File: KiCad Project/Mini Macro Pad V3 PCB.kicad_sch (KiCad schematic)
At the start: 98 parts, among them J1 USB_C_Receptacle_USB2.0_14P, SW1 SW_Push bootsel, SW10 SW_Push, SW11 SW_Push, SW12 SW_Push, SW13 SW_Push, SW14 SW_Push, SW15 SW_Push, SW16 SW_Push, SW17 SW_Push, SW18 SW_Push, SW19 SW_Push, SW2 SW_Push, SW20 SW_Push, SW21 SW_Push, SW22 RotaryEncoder_Switch_MP, SW23 RotaryEncoder_Switch_MP, SW3 SW_Push, SW4 SW_Push, SW5 SW_Push, SW6 SW_Push, SW7 SW_Push, SW8 SW_Push, SW9 SW_Push, U1 RP2040, U2 NCP1117-3.3_SOT223, U3 W25Q128JVS, Y1 ABM8-272-T3

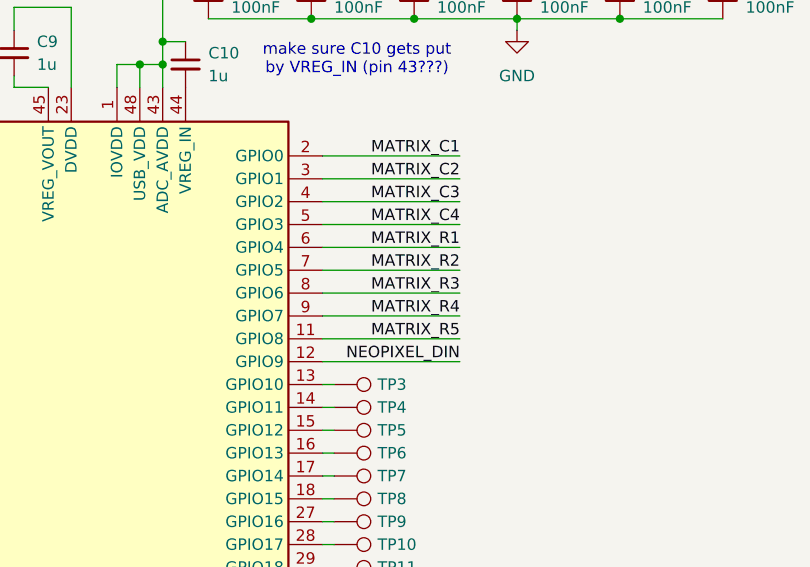
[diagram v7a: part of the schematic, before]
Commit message: changed some GPIO connections & did more trace routing
Reversed the order that C1 to C5 connect in
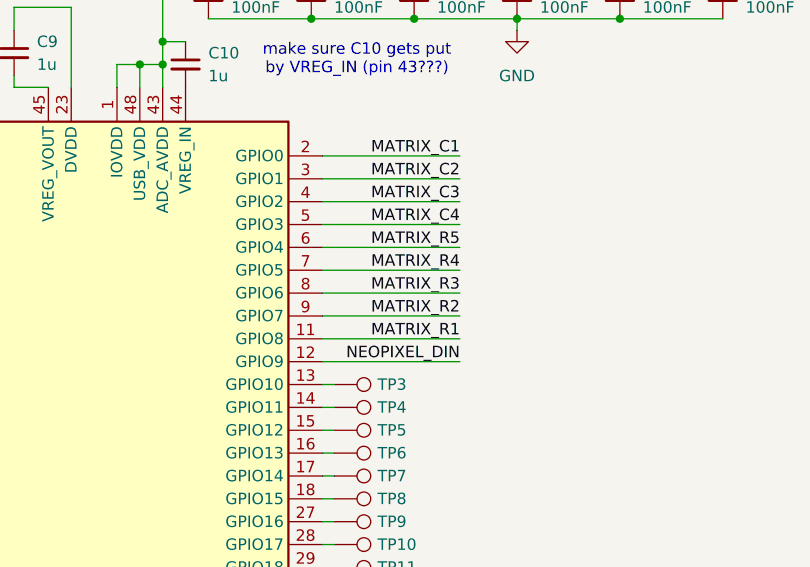
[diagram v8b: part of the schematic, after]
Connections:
- net MATRIX_R1: now also U1.11 (GPIO8); no longer U1.6 (GPIO4)
- net MATRIX_R2: now also U1.9 (GPIO7); no longer U1.7 (GPIO5)
- net MATRIX_R4: now also U1.7 (GPIO5); no longer U1.9 (GPIO7)
- net MATRIX_R5: now also U1.6 (GPIO4); no longer U1.11 (GPIO8)
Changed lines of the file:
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@@
+		)
+	)
+	(label "MATRIX_R2"
+		(at 246.38 88.9 180)
+		(effects
+			(font
+				(size 1.27 1.27)
+			)
+			(justify right bottom)
 		)
 	)
@@
 		)
 	)
-	(label "MATRIX_R4"
-		(at 246.38 88.9 180)
+	(label "MATRIX_R3"
+		(at 246.38 86.36 180)
 		(effects
 			(font
@@
 		)
 	)
-	(label "MATRIX_R5"
-		(at 246.38 91.44 180)
-		(effects
-			(font
-				(size 1.27 1.27)
-			)
-			(justify right bottom)
-		)
-	)
 	(label "MATRIX_C1"
 		(at 96.52 140.97 270)
@@
 		)
 	)
+	(label "MATRIX_R4"
+		(at 246.38 83.82 180)
+		(effects
+			(font
+				(size 1.27 1.27)
+			)
+			(justify right bottom)
+		)
+	)
 	(label "USB_D-"
 		(at 54.61 167.64 180)
@@
 	)
 	(label "MATRIX_R1"
-		(at 246.38 81.28 180)
+		(at 246.38 91.44 180)
 		(effects
 			(font
@@
 		)
 	)
-	(label "MATRIX_R3"
-		(at 246.38 86.36 180)
-		(effects
-			(font
-				(size 1.27 1.27)
-			)
-			(justify right bottom)
-		)
-	)
 	(label "ENCODER_1_B"
 		(at 246.38 124.46 180)
@@
 		)
 	)
+	(label "MATRIX_R5"
+		(at 246.38 81.28 180)
+		(effects
+			(font
+				(size 1.27 1.27)
+			)
+			(justify right bottom)
+		)
+	)
 	(label "MATRIX_C4"
 		(at 134.62 140.97 270)
@@
 		)
 	)
-	(label "MATRIX_R2"
-		(at 246.38 83.82 180)
-		(effects
-			(font
-				(size 1.27 1.27)
-			)
-			(justify right bottom)
-		)
-	)
